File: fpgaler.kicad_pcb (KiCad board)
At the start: 4 copper layers, 100 x 100 mm, 286 parts, among them J1 USB_C_Receptacle_USB2.0, J3 JTAG, J4 FTDI_RST, J5 VGA, J6 DB9 Expander, J7 DB9 Expander, Q1 BC817, SW1 RotaryEncoder_Switch, SW2 RotaryEncoder_Switch, SW3 K1, SW4 K2, SW5 PROGRAMN, SW6 K3, SW7 FPGA GSRN, SW8 K4, U1 TLV62569DRL, U10 XC6206PxxxMR, U11 IS62WV51216BLL-55TLI, U2 TLV62569DRL, U3 NCP115-2.5, U5 93LC56BT-I/OT, U6 FT2232HL, U7 CAT24C128, U8 LFE5U-25F-8MG285C, U9 W25Q128JVP, X1 27MHz, Y1 7M-12.000MAAJ

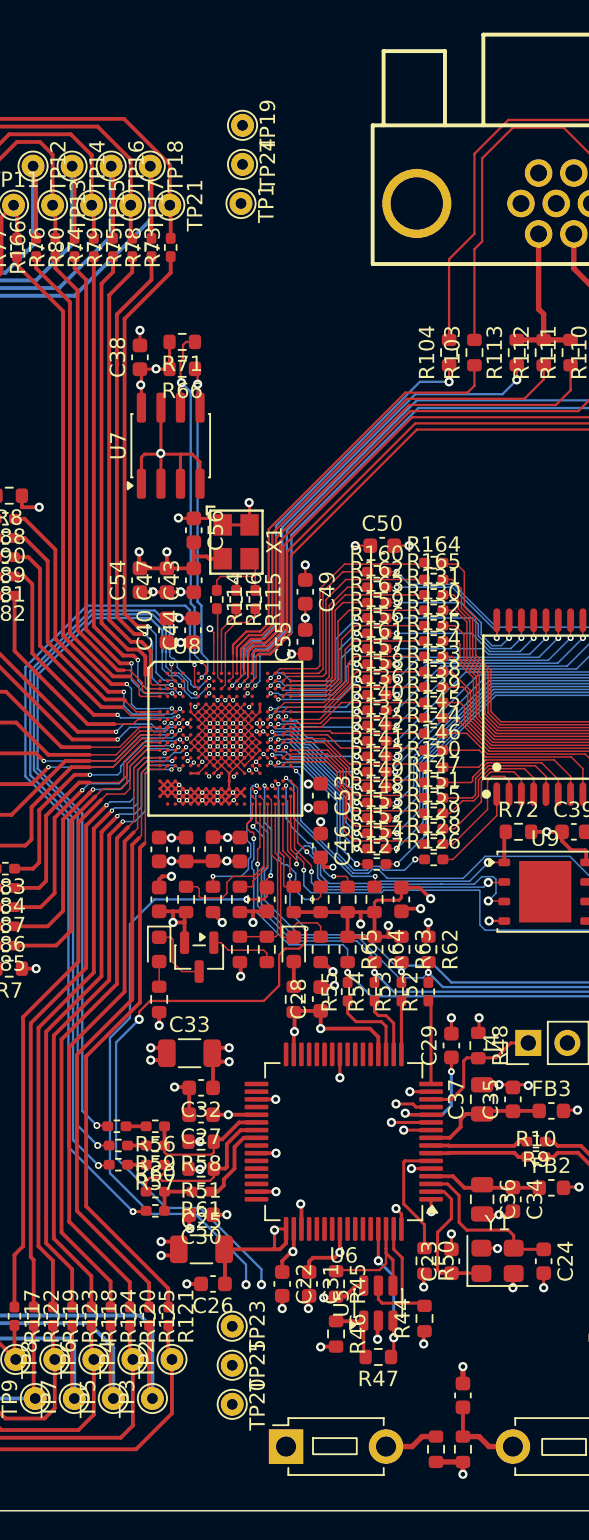
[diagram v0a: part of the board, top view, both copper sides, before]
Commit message: Fix dcr for schematics
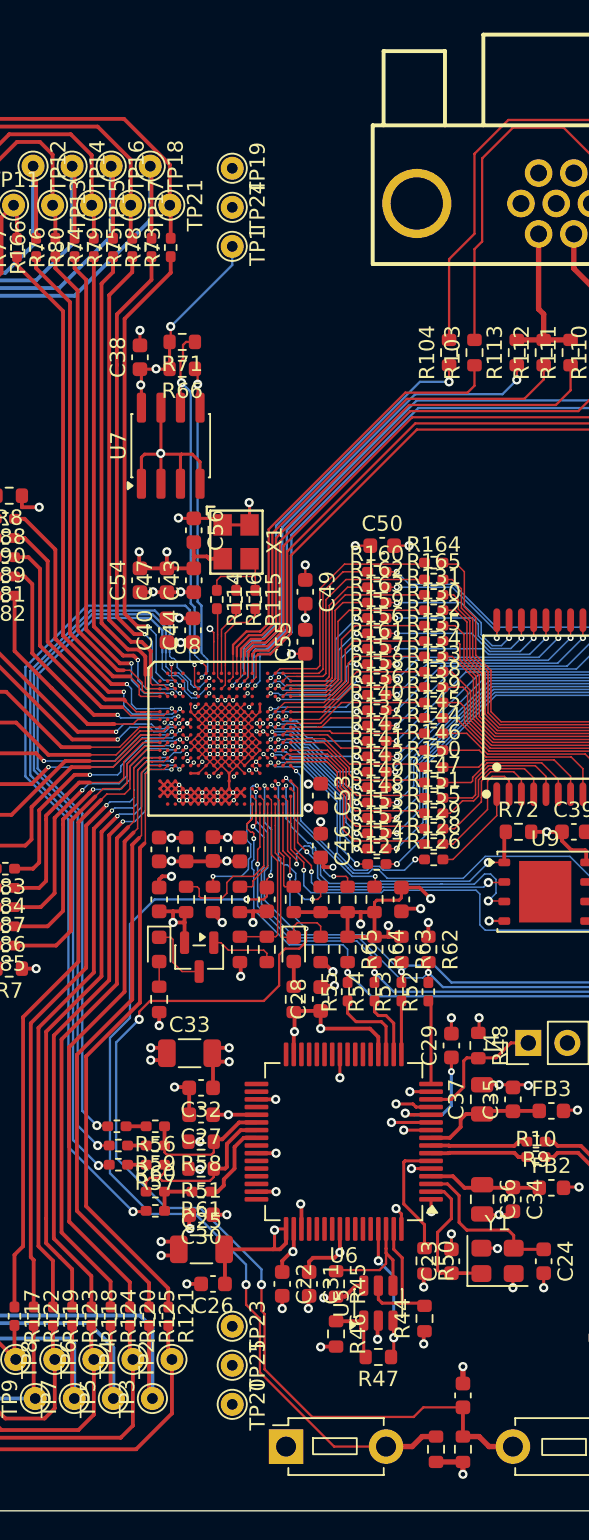
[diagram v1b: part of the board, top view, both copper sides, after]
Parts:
- moved TP19 2.87 mm to (133.0, 57.7)
- moved TP24 2.87 mm to (133.0, 60.2)
- moved TP1 2.85 mm to (133.0, 62.8)
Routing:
- net GND: track 896.1 -> 1059.2 mm
- net +2.5V: track 64.9 -> 141.8 mm
- net +3.3V: track 526.3 -> 590.5 mm, vias 68 -> 69
- net +1.1V: track 37.6 -> 77.3 mm
- net /GSRN: track 52.5 -> 72.5 mm
- net /PROGRAMN: track 50.5 -> 66.8 mm
